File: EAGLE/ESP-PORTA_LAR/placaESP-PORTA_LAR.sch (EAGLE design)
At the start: 21 parts

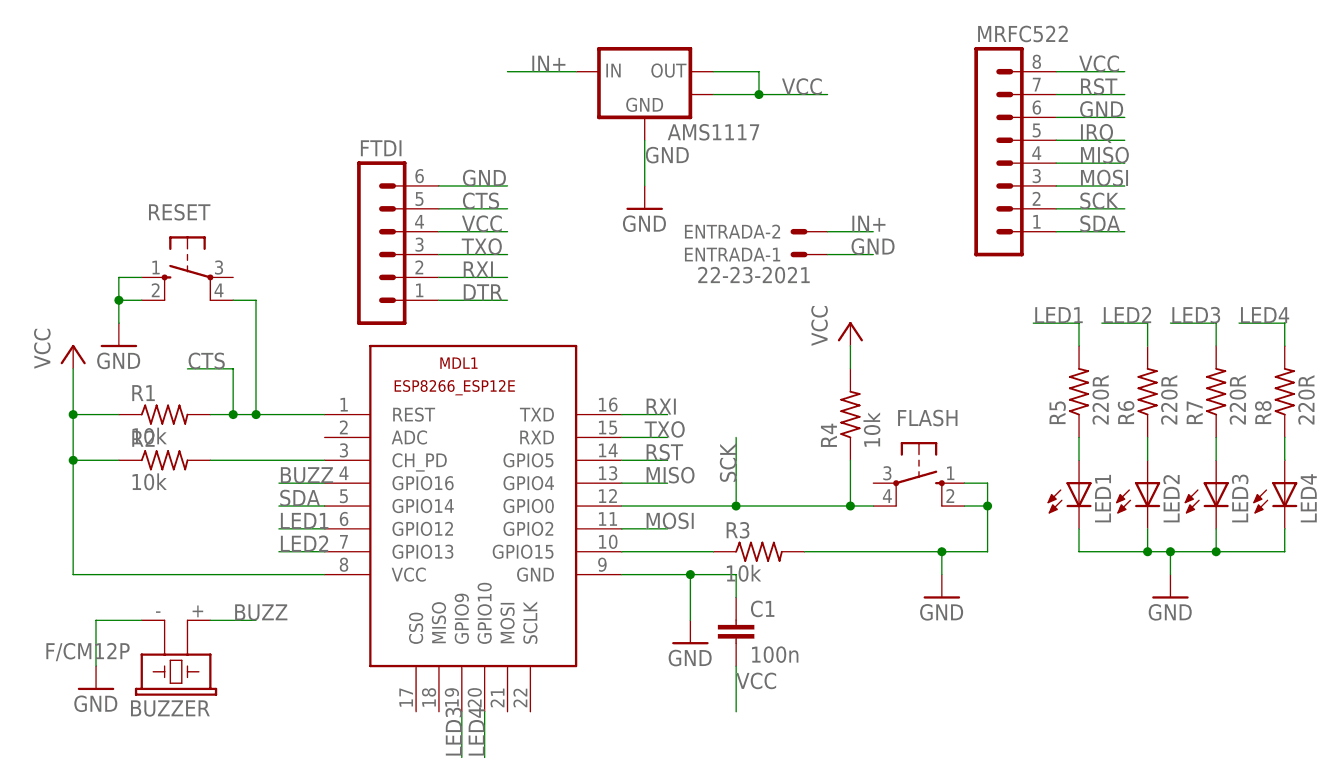
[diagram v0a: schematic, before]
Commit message: Mudanças na placa
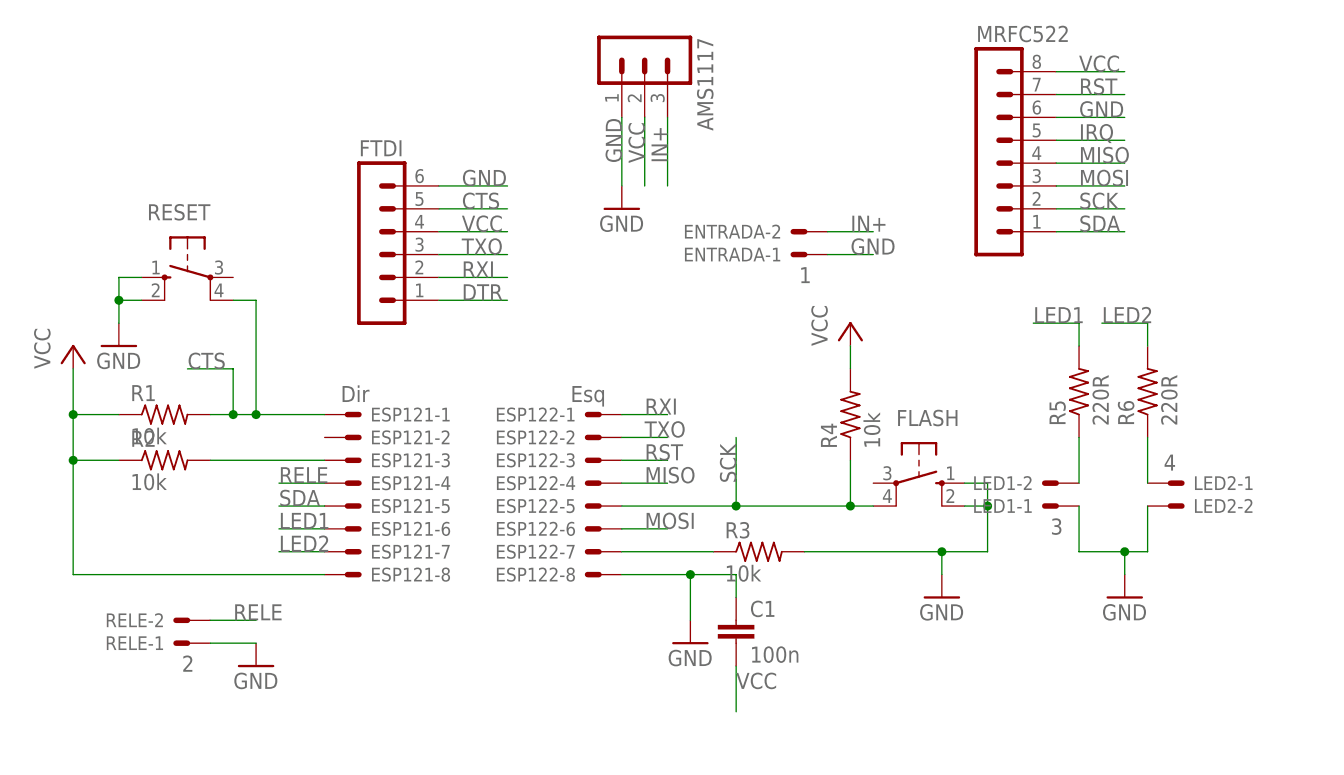
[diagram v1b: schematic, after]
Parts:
- removed BUZZER: F/CM12P, buzzer:F/CM12P
- removed LED3, LED4: (no value), led:LED3MM
- removed MDL1: (no value), ESP8266-ESP12E:ESP8266-12EESP8266-ESP12E
- removed R7, R8: 220R, resistor:R-US_0207/10
- added ESP121: Dir, con-molex:22-23-2081
- added ESP122: Esq, con-molex:22-23-2081
- added RELE: 2, con-molex:22-23-2021
- AMS1117: device kaibader:AMS1117 -> con-lstb:MA03-1
- ENTRADA: value 22-23-2021 -> 1
- LED1: value (none) -> 3; device led:LED3MM -> con-molex:22-23-2021
- LED2: value (none) -> 4; device led:LED3MM -> con-molex:22-23-2021
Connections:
- removed net BUZZ: BUZZER.1, MDL1.GPIO16
- removed net LED3: MDL1.GPIO9, R7.2
- removed net LED4: MDL1.GPIO10, R8.2
- removed net N$7: LED3.A, R7.1
- removed net N$8: LED4.A, R8.1
- new net RELE: ESP121-4.S, RELE-2.S
- net CTS: now also ESP121-1.S; no longer MDL1.REST
- net GND: now also AMS1117.1, ESP122-8.S, LED1-1.S, LED2-2.S, RELE-1.S; no longer AMS1117.ADJ-GND, BUZZER.2, LED1.C, LED2.C, LED3.C, LED4.C, MDL1.GND
- net IN+: now also AMS1117.3; no longer AMS1117.VIN
- net LED1: now also ESP121-6.S; no longer MDL1.GPIO12
- net LED2: now also ESP121-7.S; no longer MDL1.GPIO13
- net MISO: now also ESP122-4.S; no longer MDL1.GPIO4
- net MOSI: now also ESP122-6.S; no longer MDL1.GPIO2
- net N$1: now also ESP122-7.S; no longer MDL1.GPIO15
- net N$3: now also ESP121-3.S; no longer MDL1.CH_PD
- net N$5: now also LED1-2.S; no longer LED1.A
- net N$6: now also LED2-1.S; no longer LED2.A
- net RST: now also ESP122-3.S; no longer MDL1.GPIO5
- net RXI: now also ESP122-1.S; no longer MDL1.TXD
- net SCK: now also ESP122-5.S; no longer MDL1.GPIO0
- net SDA: now also ESP121-5.S; no longer MDL1.GPIO14
- net TXO: now also ESP122-2.S; no longer MDL1.RXD
- net VCC: now also AMS1117.2, ESP121-8.S; no longer AMS1117.HEATSINK, AMS1117.VOUT, MDL1.VCC

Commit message: Nova Placa
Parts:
- ENTRADA: value 1 -> (none); device con-molex:22-23-2021 -> con-jack:JACK-PLUG0
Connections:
- removed net N$6: LED2-1.S, R6.1
- new net N$2: LED2-2.S, R6.1
- net GND: now also ENTRADA.1, ENTRADA.2, LED2-1.S; no longer ENTRADA-1.S, LED2-2.S
- net IN+: now also ENTRADA.3; no longer ENTRADA-2.S
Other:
- moved on the sheet: LED2-1, LED2-2
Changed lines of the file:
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@@
 <part name="FLASH" library="switch-omron" deviceset="10-XX" device=""/>
 <part name="RESET" library="switch-omron" deviceset="10-XX" device=""/>
-<part name="ENTRADA" library="con-molex" deviceset="22-23-2021" device="" value="1"/>
 <part name="P+1" library="supply1" deviceset="VCC" device=""/>
 <part name="GND1" library="supply1" deviceset="GND" device=""/>
@@
 <part name="LED1" library="con-molex" deviceset="22-23-2021" device="" value="3"/>
 <part name="LED2" library="con-molex" deviceset="22-23-2021" device="" value="4"/>
+<part name="ENTRADA" library="con-jack" library_urn="urn:adsk.eagle:library:154" deviceset="JACK-PLUG" device="0" package3d_urn="urn:adsk.eagle:package:7492/1"/>
 </parts>
 <sheets>
@@
 <instance part="FLASH" gate="1" x="63.5" y="60.96" rot="R270"/>
 <instance part="RESET" gate="1" x="-17.78" y="83.82" rot="MR270"/>
-<instance part="ENTRADA" gate="-1" x="50.8" y="86.36" rot="R180"/>
-<instance part="ENTRADA" gate="-2" x="50.8" y="88.9" rot="R180"/>
 <instance part="P+1" gate="VCC" x="-30.48" y="76.2"/>
 <instance part="GND1" gate="1" x="-25.4" y="76.2"/>
@@
 <instance part="LED1" gate="-1" x="78.74" y="58.42" rot="R180"/>
 <instance part="LED1" gate="-2" x="78.74" y="60.96" rot="R180"/>
-<instance part="LED2" gate="-1" x="91.44" y="60.96"/>
-<instance part="LED2" gate="-2" x="91.44" y="58.42"/>
+<instance part="LED2" gate="-1" x="91.44" y="58.42"/>
+<instance part="LED2" gate="-2" x="91.44" y="60.96"/>
+<instance part="ENTRADA" gate="G$1" x="48.26" y="86.36"/>
 </instances>
 <busses>
@@
 </segment>
 <segment>
-<pinref part="ENTRADA" gate="-1" pin="S"/>
-<wire x1="53.34" y1="86.36" x2="58.42" y2="86.36" width="0.1524" layer="91"/>
-<label x="55.88" y="86.36" size="1.778" layer="95"/>
+<label x="60.96" y="86.36" size="1.778" layer="95"/>
+<pinref part="ENTRADA" gate="G$1" pin="2"/>
+<wire x1="53.34" y1="86.36" x2="55.88" y2="86.36" width="0.1524" layer="91"/>
+<pinref part="ENTRADA" gate="G$1" pin="1"/>
+<wire x1="55.88" y1="86.36" x2="63.5" y2="86.36" width="0.1524" layer="91"/>
+<wire x1="53.34" y1="83.82" x2="55.88" y2="83.82" width="0.1524" layer="91"/>
+<wire x1="55.88" y1="83.82" x2="55.88" y2="86.36" width="0.1524" layer="91"/>
+<junction x="55.88" y="86.36"/>
 </segment>
 <segment>
@@
 <pinref part="LED1" gate="-1" pin="S"/>
 <wire x1="81.28" y1="58.42" x2="81.28" y2="53.34" width="0.1524" layer="91"/>
-<pinref part="LED2" gate="-2" pin="S"/>
+<pinref part="LED2" gate="-1" pin="S"/>
 <wire x1="88.9" y1="58.42" x2="88.9" y2="53.34" width="0.1524" layer="91"/>
 </segment>
@@
 <net name="IN+" class="0">
 <segment>
-<pinref part="ENTRADA" gate="-2" pin="S"/>
-<wire x1="53.34" y1="88.9" x2="58.42" y2="88.9" width="0.1524" layer="91"/>
-<label x="55.88" y="88.9" size="1.778" layer="95"/>
+<label x="60.96" y="88.9" size="1.778" layer="95"/>
+<pinref part="ENTRADA" gate="G$1" pin="3"/>
+<wire x1="53.34" y1="88.9" x2="63.5" y2="88.9" width="0.1524" layer="91"/>
 </segment>
 <segment>
@@
 </segment>
 </net>
-<net name="N$6" class="0">
-<segment>
-<pinref part="R6" gate="G$1" pin="1"/>
-<pinref part="LED2" gate="-1" pin="S"/>
-<wire x1="88.9" y1="60.96" x2="88.9" y2="66.04" width="0.1524" layer="91"/>
-</segment>
-</net>
 <net name="RELE" class="0">
 <segment>
@@
 </segment>
 </net>
+<net name="N$2" class="0">
+<segment>
+<pinref part="LED2" gate="-2" pin="S"/>
+<pinref part="R6" gate="G$1" pin="1"/>
+<wire x1="88.9" y1="60.96" x2="88.9" y2="66.04" width="0.1524" layer="91"/>
+</segment>
+</net>

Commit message: Últimas modificações
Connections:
- net GND: no longer FLASH.S1
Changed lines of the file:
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@@
 <pinref part="FLASH" gate="1" pin="S"/>
 <wire x1="68.58" y1="60.96" x2="71.12" y2="60.96" width="0.1524" layer="91"/>
-<wire x1="71.12" y1="60.96" x2="71.12" y2="58.42" width="0.1524" layer="91"/>
-<pinref part="FLASH" gate="1" pin="S1"/>
-<wire x1="71.12" y1="58.42" x2="68.58" y2="58.42" width="0.1524" layer="91"/>
-<wire x1="71.12" y1="58.42" x2="71.12" y2="53.34" width="0.1524" layer="91"/>
-<junction x="71.12" y="58.42"/>
+<wire x1="71.12" y1="60.96" x2="71.12" y2="53.34" width="0.1524" layer="91"/>
 <wire x1="71.12" y1="53.34" x2="66.04" y2="53.34" width="0.1524" layer="91"/>
 <junction x="66.04" y="53.34"/>

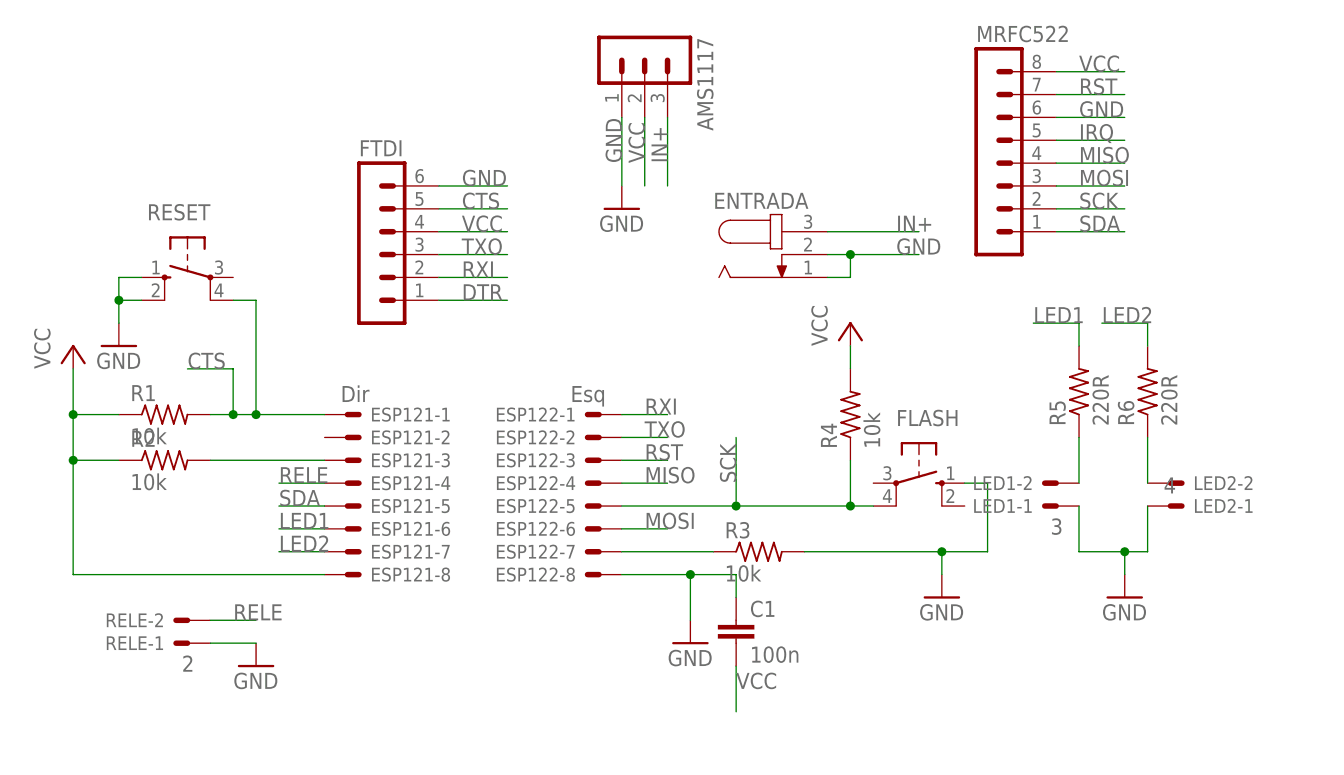
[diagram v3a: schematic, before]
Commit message: Revert "Mais mod. na placa da porta"
This reverts commit dd03839187e335b1d892b75bb02f8486d9d1b679.
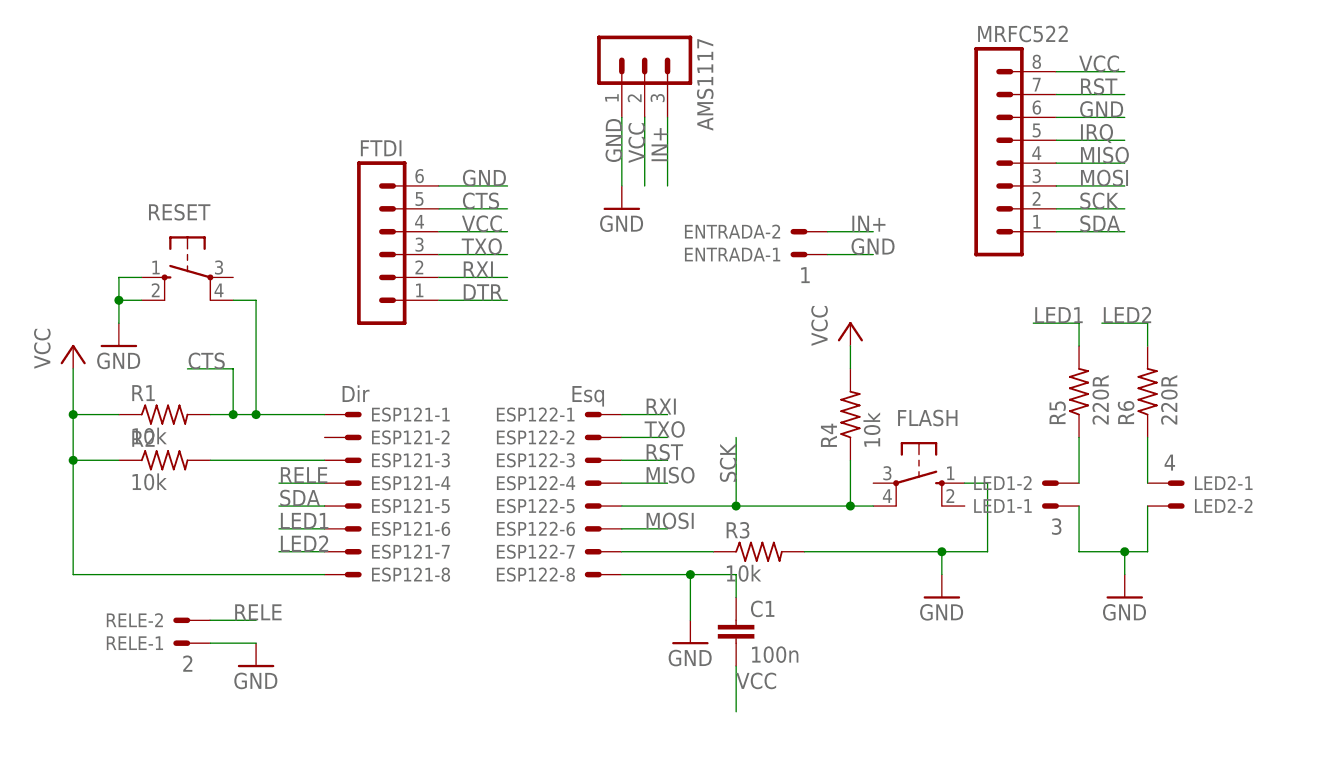
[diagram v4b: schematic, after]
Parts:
- ENTRADA: value (none) -> 1; device con-jack:JACK-PLUG0 -> con-molex:22-23-2021
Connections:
- removed net N$2: LED2-2.S, R6.1
- new net N$6: LED2-1.S, R6.1
- net GND: now also ENTRADA-1.S, LED2-2.S; no longer ENTRADA.1, ENTRADA.2, LED2-1.S
- net IN+: now also ENTRADA-2.S; no longer ENTRADA.3
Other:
- moved on the sheet: LED2-1, LED2-2
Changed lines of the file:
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@@
 <part name="FLASH" library="switch-omron" deviceset="10-XX" device=""/>
 <part name="RESET" library="switch-omron" deviceset="10-XX" device=""/>
+<part name="ENTRADA" library="con-molex" deviceset="22-23-2021" device="" value="1"/>
 <part name="P+1" library="supply1" deviceset="VCC" device=""/>
 <part name="GND1" library="supply1" deviceset="GND" device=""/>
@@
 <part name="LED1" library="con-molex" deviceset="22-23-2021" device="" value="3"/>
 <part name="LED2" library="con-molex" deviceset="22-23-2021" device="" value="4"/>
-<part name="ENTRADA" library="con-jack" library_urn="urn:adsk.eagle:library:154" deviceset="JACK-PLUG" device="0" package3d_urn="urn:adsk.eagle:package:7492/1"/>
 </parts>
 <sheets>
@@
 <instance part="FLASH" gate="1" x="63.5" y="60.96" rot="R270"/>
 <instance part="RESET" gate="1" x="-17.78" y="83.82" rot="MR270"/>
+<instance part="ENTRADA" gate="-1" x="50.8" y="86.36" rot="R180"/>
+<instance part="ENTRADA" gate="-2" x="50.8" y="88.9" rot="R180"/>
 <instance part="P+1" gate="VCC" x="-30.48" y="76.2"/>
 <instance part="GND1" gate="1" x="-25.4" y="76.2"/>
@@
 <instance part="LED1" gate="-1" x="78.74" y="58.42" rot="R180"/>
 <instance part="LED1" gate="-2" x="78.74" y="60.96" rot="R180"/>
-<instance part="LED2" gate="-1" x="91.44" y="58.42"/>
-<instance part="LED2" gate="-2" x="91.44" y="60.96"/>
-<instance part="ENTRADA" gate="G$1" x="48.26" y="86.36"/>
+<instance part="LED2" gate="-1" x="91.44" y="60.96"/>
+<instance part="LED2" gate="-2" x="91.44" y="58.42"/>
 </instances>
 <busses>
@@
 </segment>
 <segment>
-<label x="60.96" y="86.36" size="1.778" layer="95"/>
-<pinref part="ENTRADA" gate="G$1" pin="2"/>
-<wire x1="53.34" y1="86.36" x2="55.88" y2="86.36" width="0.1524" layer="91"/>
-<pinref part="ENTRADA" gate="G$1" pin="1"/>
-<wire x1="55.88" y1="86.36" x2="63.5" y2="86.36" width="0.1524" layer="91"/>
-<wire x1="53.34" y1="83.82" x2="55.88" y2="83.82" width="0.1524" layer="91"/>
-<wire x1="55.88" y1="83.82" x2="55.88" y2="86.36" width="0.1524" layer="91"/>
-<junction x="55.88" y="86.36"/>
+<pinref part="ENTRADA" gate="-1" pin="S"/>
+<wire x1="53.34" y1="86.36" x2="58.42" y2="86.36" width="0.1524" layer="91"/>
+<label x="55.88" y="86.36" size="1.778" layer="95"/>
 </segment>
 <segment>
@@
 <pinref part="LED1" gate="-1" pin="S"/>
 <wire x1="81.28" y1="58.42" x2="81.28" y2="53.34" width="0.1524" layer="91"/>
-<pinref part="LED2" gate="-1" pin="S"/>
+<pinref part="LED2" gate="-2" pin="S"/>
 <wire x1="88.9" y1="58.42" x2="88.9" y2="53.34" width="0.1524" layer="91"/>
 </segment>
@@
 <net name="IN+" class="0">
 <segment>
-<label x="60.96" y="88.9" size="1.778" layer="95"/>
-<pinref part="ENTRADA" gate="G$1" pin="3"/>
-<wire x1="53.34" y1="88.9" x2="63.5" y2="88.9" width="0.1524" layer="91"/>
+<pinref part="ENTRADA" gate="-2" pin="S"/>
+<wire x1="53.34" y1="88.9" x2="58.42" y2="88.9" width="0.1524" layer="91"/>
+<label x="55.88" y="88.9" size="1.778" layer="95"/>
 </segment>
 <segment>
@@
 </segment>
 </net>
+<net name="N$6" class="0">
+<segment>
+<pinref part="R6" gate="G$1" pin="1"/>
+<pinref part="LED2" gate="-1" pin="S"/>
+<wire x1="88.9" y1="60.96" x2="88.9" y2="66.04" width="0.1524" layer="91"/>
+</segment>
+</net>
 <net name="RELE" class="0">
 <segment>
@@
 </segment>
 </net>
-<net name="N$2" class="0">
-<segment>
-<pinref part="LED2" gate="-2" pin="S"/>
-<pinref part="R6" gate="G$1" pin="1"/>
-<wire x1="88.9" y1="60.96" x2="88.9" y2="66.04" width="0.1524" layer="91"/>
-</segment>
-</net>
